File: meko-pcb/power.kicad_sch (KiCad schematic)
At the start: 28 parts, among them IC3 LP5912-3.3DRVR, U10 LP5907SNX-1.8/NOPB, U2 TP4056-42-ESOP8, U3 LP5907SNX-3.3/NOPB, U4 LP5907SNX-3.3/NOPB, U6 LP5907SNX-3.3/NOPB, U7 LP5907SNX-1.8/NOPB

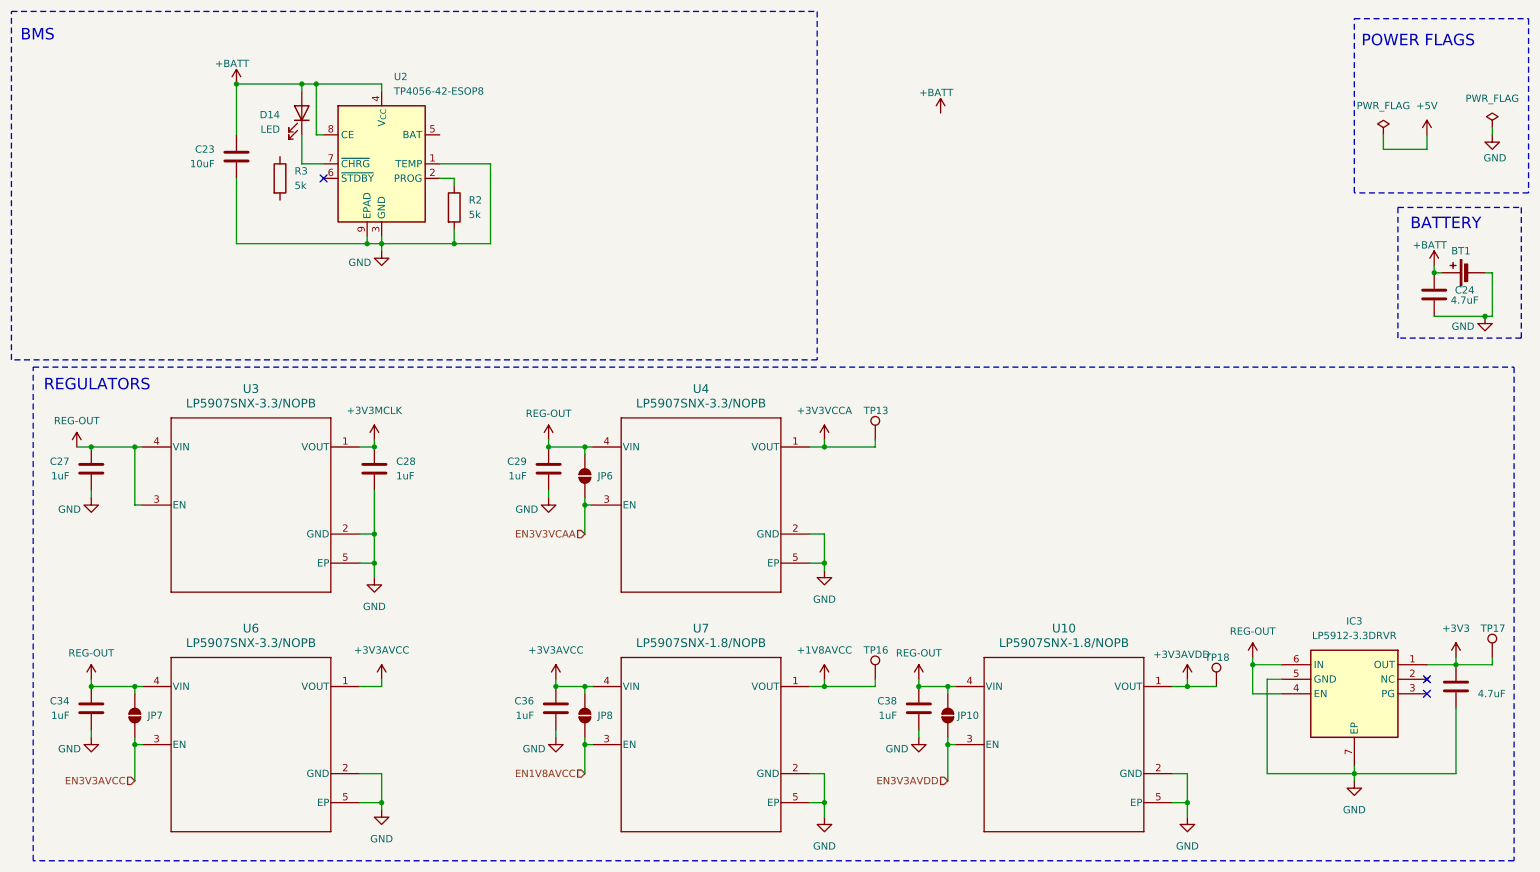
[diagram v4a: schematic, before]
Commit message: started to implement npm1300
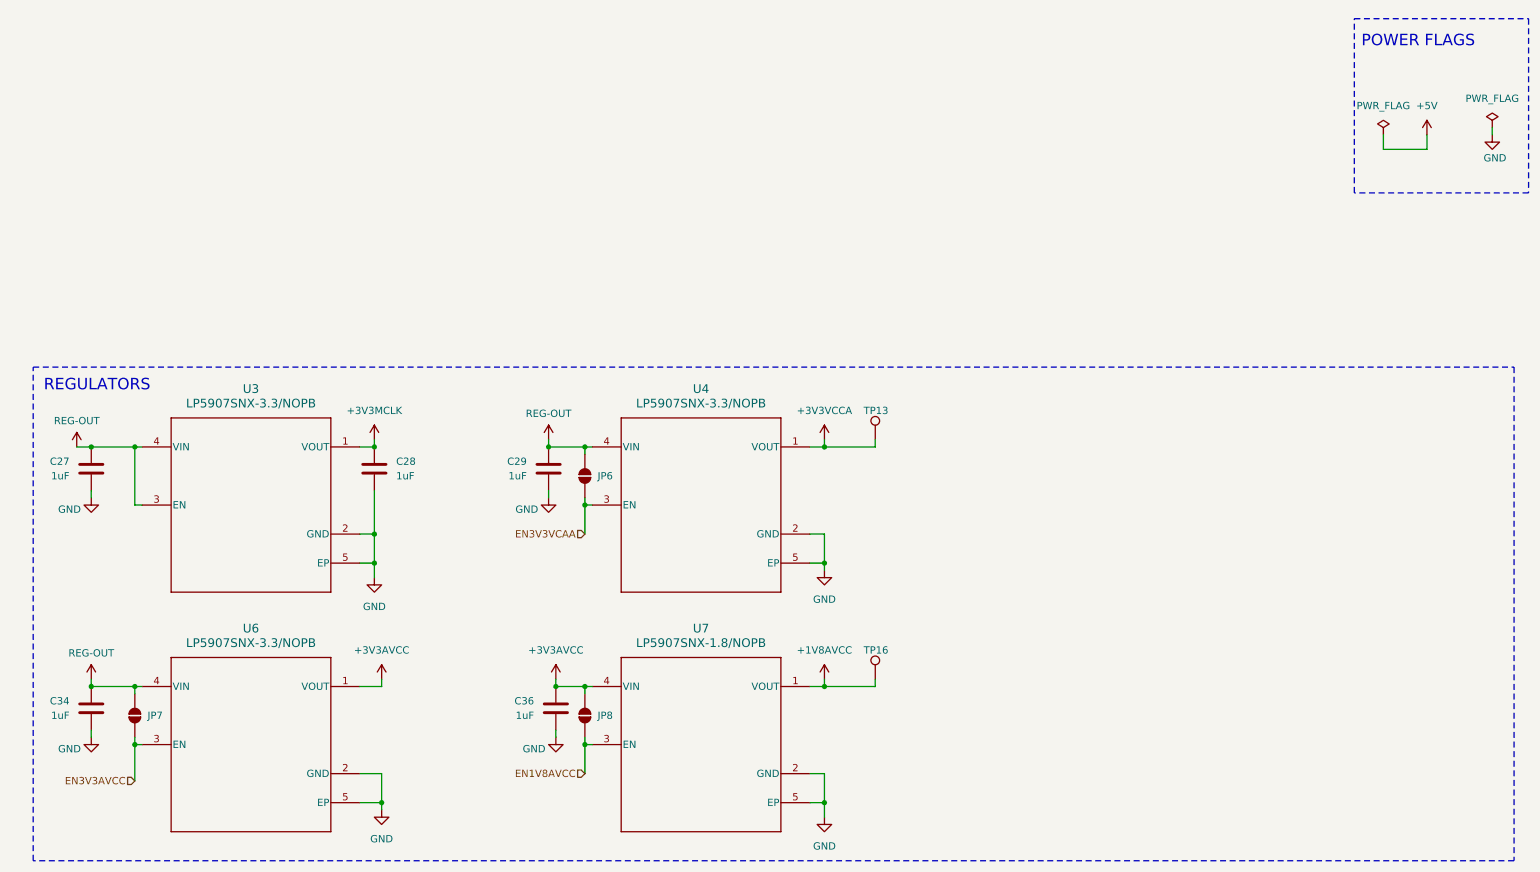
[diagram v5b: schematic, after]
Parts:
- removed BT1: Battery_Cell, S2B-PH-SM4-TB_LF__SN_:JST_S2B-PH-SM4-TB_LF__SN_, symbol Device:Battery_Cell
- removed C23: 10uF, symbol Device:C
- removed C24, C33: 4.7uF, Capacitor_SMD:C_0402_1005Metric, symbol Device:C
- removed C38: 1uF, Capacitor_SMD:C_0402_1005Metric, symbol Device:C
- removed D14: LED, LED_SMD:LED_0603_1608Metric, symbol Device:LED
- removed IC3: LP5912-3.3DRVR, LP5912-3.3DRVR:SON65P200X200X80-7N, symbol LP5912-3_3DRVR:LP5912-3.3DRVR
- removed JP10: SolderJumper_2_Open, Jumper:SolderJumper-2_P1.3mm_Open_RoundedPad1.0x1.5mm, symbol Jumper:SolderJumper_2_Open
- removed R2, R3: 5k, symbol Device:R
- removed TP17, TP18: TestPoint, TestPoint:TestPoint_Pad_D1.0mm, symbol Connector:TestPoint
- removed U10: LP5907SNX-1.8/NOPB, Package_SON:Texas_X2SON-4_1x1mm_P0.65mm, symbol LP5907SNX-1-8-NOPB:LP5907SNX-1.8_NOPB
- removed U2: TP4056-42-ESOP8, Package_SO:SOIC-8-1EP_3.9x4.9mm_P1.27mm_EP2.41x3.3mm_ThermalVias, symbol Battery_Management:TP4056-42-ESOP8
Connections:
- no-connect marks 3 -> 0
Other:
- note removed: "BATTERY"
- note removed: "BMS"

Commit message: added new ldos, made improvements to the schematic
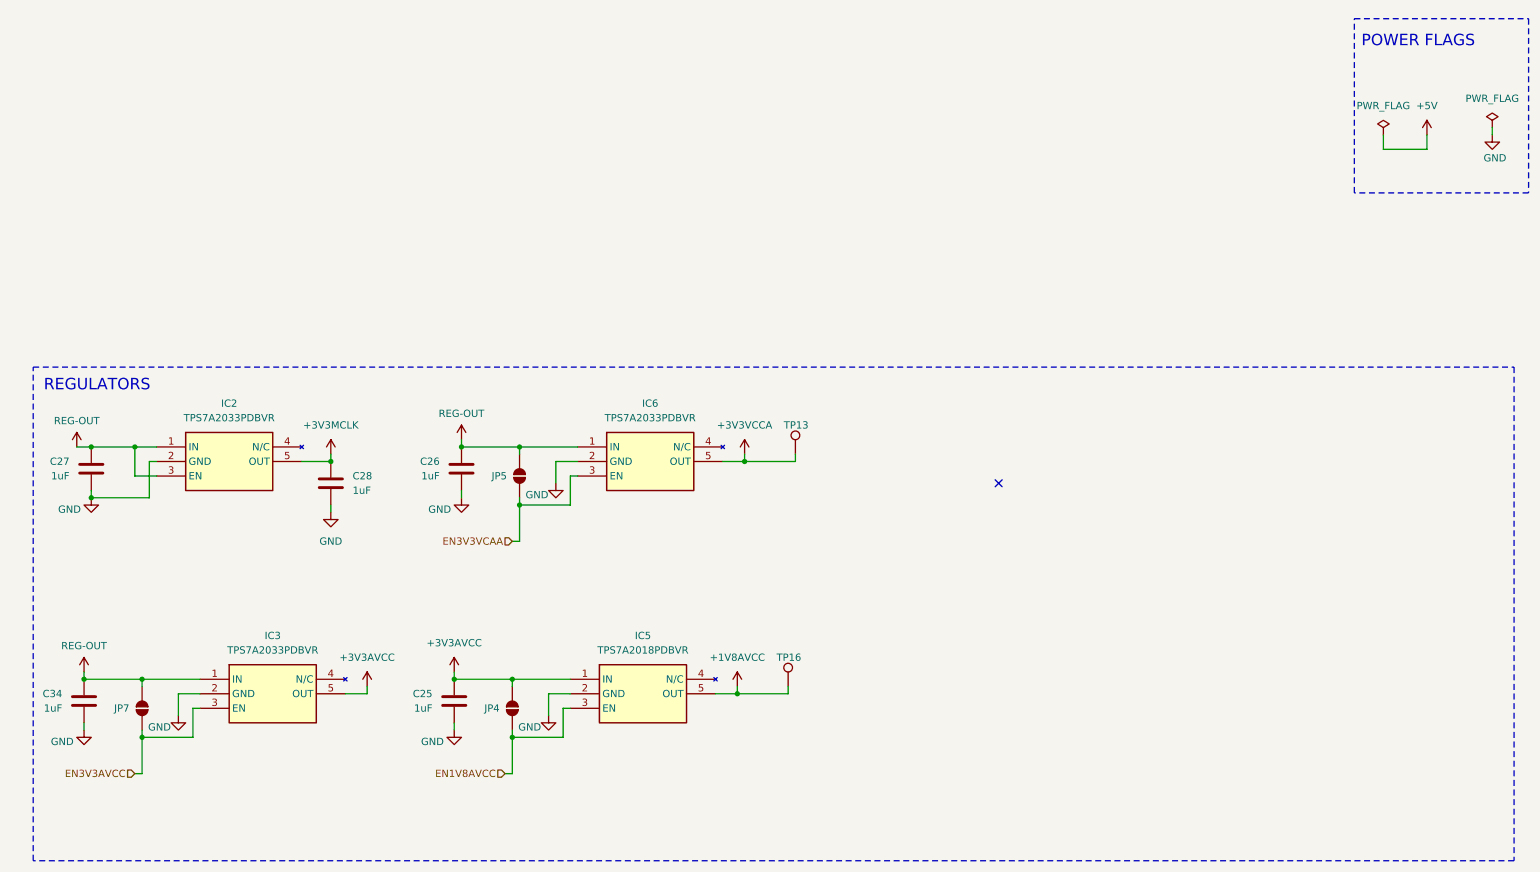
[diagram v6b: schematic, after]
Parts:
- removed C29, C36: 1uF, Capacitor_SMD:C_0402_1005Metric, symbol Device:C
- removed JP6, JP8: SolderJumper_2_Open, Jumper:SolderJumper-2_P1.3mm_Open_RoundedPad1.0x1.5mm, symbol Jumper:SolderJumper_2_Open
- removed U3, U4, U6: LP5907SNX-3.3/NOPB, Package_SON:Texas_X2SON-4_1x1mm_P0.65mm, symbol LP5907SNX-3-3-NOPB:LP5907SNX-3.3_NOPB
- removed U7: LP5907SNX-1.8/NOPB, Package_SON:Texas_X2SON-4_1x1mm_P0.65mm, symbol LP5907SNX-1-8-NOPB:LP5907SNX-1.8_NOPB
- added C25, C26: 1uF, Capacitor_SMD:C_0402_1005Metric, symbol Device:C
- added IC2, IC3, IC6: TPS7A2033PDBVR, TPS7A2018PDBVR:SOT95P280X145-5N, symbol TPS7A2033PDBVR:TPS7A2033PDBVR
- added IC5: TPS7A2018PDBVR, TPS7A2018PDBVR:SOT95P280X145-5N, symbol TPS7A2018PDBVR:TPS7A2018PDBVR
- added JP4, JP5: SolderJumper_2_Open, Jumper:SolderJumper-2_P1.3mm_Open_RoundedPad1.0x1.5mm, symbol Jumper:SolderJumper_2_Open
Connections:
- net +1V8AVCC: now also IC5.5 (OUT)
- net +3V3AVCC: now also C25.1, IC3.5 (OUT), IC5.1 (IN), JP4.1 (A)
- net +3V3MCLK: now also IC2.5 (OUT)
- net +3V3VCCA: now also IC6.5 (OUT)
- net EN1V8AVCC: now also IC5.3 (EN), JP4.2 (B)
- net EN3V3AVCC: now also IC3.3 (EN)
- net EN3V3VCAA: now also IC6.3 (EN), JP5.2 (B)
- net GND: now also C25.2, C26.2, IC2.2 (GND), IC3.2 (GND), IC5.2 (GND), IC6.2 (GND)
- net REG-OUT: now also C26.1, IC2.1 (IN), IC2.3 (EN), IC3.1 (IN), IC6.1 (IN), JP5.1 (A)
- no-connect marks 0 -> 1
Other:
- moved on the sheet: C28, C34, JP7, TP13, TP16
